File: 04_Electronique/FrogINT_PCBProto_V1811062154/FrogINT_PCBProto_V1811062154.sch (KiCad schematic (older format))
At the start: 3 parts

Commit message: Creation d'une version Draft du schéma
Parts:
- added C? (x2): 22pF, symbol Device:C
- added C? (x2): 0.1µF, symbol Device:C
- added D? (x3): WS2812B, LED_SMD:LED_WS2812B_PLCC4_5.0x5.0mm_P3.2mm, symbol LED:WS2812B
- added J?: AVR-JTAG-10, symbol Connector:AVR-JTAG-10
- added J?: USB_B_Mini, symbol Connector_FTA:USB_B_Mini
- added R?: 10k, symbol Device:R
- added SW?: SW_SPST, symbol Switch:SW_SPST
- added Y?: 16MHz, symbol Device:Crystal
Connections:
- net labels added: D+, D-, Input_Interrupt, reset
- wire segments 20 -> 82
- no-connect marks 2 -> 1
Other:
- note added: "By-Pass Cap"
- note added: "JTAG"
- note added: "LED RGB"
- moved on the sheet: R?, SW?

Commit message: Création version 01 du schéma pour impression Chine
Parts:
- added C1, C9: 22µF, symbol Device:CP
- added C10, C2, C3: 100nF, symbol Device:C
- added C8: 1µF, symbol Device:C
- added F1: Polyfuse MF-MSMF050-2, symbol Device:Polyfuse_Small
- added J2: Conn_01x01_Female, symbol Connector:Conn_01x01_Female
- added Q1, Q2: PMV48XP, symbol Device:Q_PMOS_DGS
- added R2, R3: 22, symbol Device:R
- added R4, R5: 10k, symbol Device:R
- added U1: NCP1117-5.0_SOT223, Package_TO_SOT_SMD:SOT-223-3_TabPin2, symbol Regulator_Linear:NCP1117-5.0_SOT223
- added U2: LP2985-3.3, Package_TO_SOT_SMD:SOT-23-5, symbol Regulator_Linear:LP2985-3.3
- J1: renamed from J?; symbol Connector_FTA:USB_B_Mini -> FrogINT_PCBProto_V1811062154-rescue:USB_B_Mini-Connector_FTA
- gave numbers to parts that had none: 14
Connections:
- net labels added: +5V, VBUS, Vin
- wire segments 82 -> 135
- no-connect marks 1 -> 2
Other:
- note added: "ATMEGA16U2"
- note added: "Power supply + By-Pass"
- note removed: "ATMega16U car possède USB et I2C"
- note removed: "Diamètre trou = 35mm"

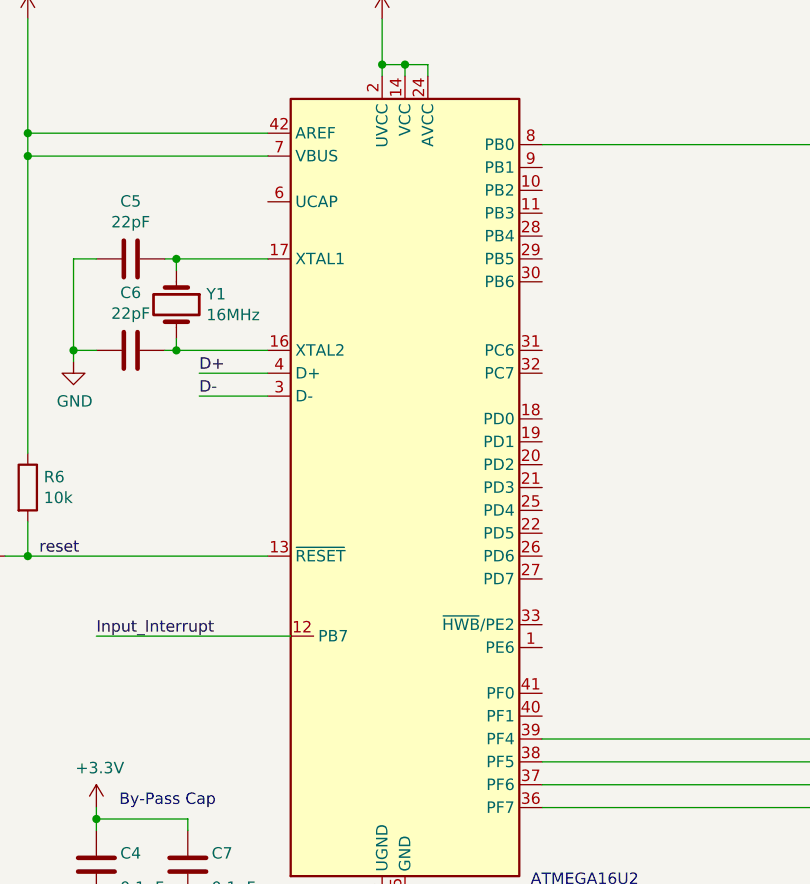
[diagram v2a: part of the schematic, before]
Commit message: First Prototype realization concerning the PCB, BOM and other manufacturing files.
This prototype could be use with Chinese partner for "Request For Quotation" process.
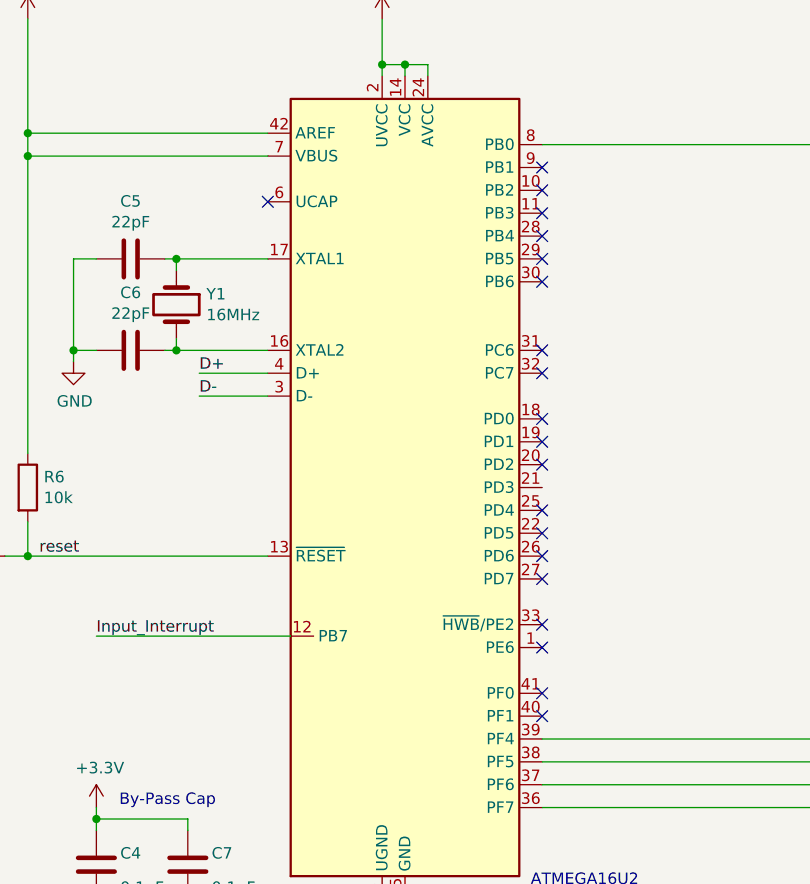
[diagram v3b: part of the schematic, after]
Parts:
- C1, C10, C2, C3, C4, C5, C6, C7, C8, C9: footprint (none) -> FTA_FrogINT_Library_Footprint_Package:CP_EIA-2012-12_Kemet-R
- D1, D2, D3: footprint LED_SMD:LED_WS2812B_PLCC4_5.0x5.0mm_P3.2mm -> FTA_FrogINT_Library_Footprint_Package:LED_WS2812B_PLCC4_5.0x5.0mm_P3.2mm
- F1: footprint (none) -> Fuse:Fuse_1206_3216Metric
- J1: footprint (none) -> Connector_USB:USB_Micro-B_Amphenol_10103594-0001LF_Horizontal
- J2: footprint (none) -> Connector_PinHeader_2.54mm:PinHeader_1x01_P2.54mm_Horizontal
- J3: footprint (none) -> FTA_FrogINT_Library_Footprint_Package:PinHeader_2x05_P2.54mm_Vertical
- Q1, Q2: footprint (none) -> Package_TO_SOT_SMD:SOT-23-6
- R1, R2, R3, R4, R5, R6: footprint (none) -> FTA_FrogINT_Library_Footprint_Package:R_0603_1608Metric
- SW1, SW2: footprint (none) -> FTA_FrogINT_Library_Footprint_Package:SW_SPST_B3S-1000
- U3: footprint Package_QFP:TQFP-44_10x10mm_P0.8mm -> FTA_FrogINT_Library_Footprint_Package:TQFP-44_10x10mm_P0.8mm
- Y1: footprint (none) -> FTA_FrogINT_Library_Footprint_Package:Crystal_HC49-U_Vertical
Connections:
- no-connect marks 2 -> 22
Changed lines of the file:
@@
 F 0 "U3" H 6100 1150 50  0000 C CNN
 F 1 "ATmega16U4RC-AU" H 6000 973 50  0001 C CNN
-F 2 "Package_QFP:TQFP-44_10x10mm_P0.8mm" H 6000 2950 50  0001 C CIN
+F 2 "FTA_FrogINT_Library_Footprint_Package:TQFP-44_10x10mm_P0.8mm" H 6000 2950 50  0001 C CIN
 F 3 "http://ww1.microchip.com/downloads/en/DeviceDoc/Atmel-7766-8-bit-AVR-ATmega16U4-32U4_Datasheet.pdf" H 6000 2950 50  0001 C CNN
 	1    6000 2950
@@
 F 0 "SW2" H 4050 3393 50  0000 C CNN
 F 1 "SW_SPST" H 4050 3394 50  0001 C CNN
-F 2 "" H 4050 3250 50  0001 C CNN
+F 2 "FTA_FrogINT_Library_Footprint_Package:SW_SPST_B3S-1000" H 4050 3250 50  0001 C CNN
 F 3 "" H 4050 3250 50  0001 C CNN
 	1    4050 3250
@@
 F 0 "R6" H 4420 2996 50  0000 L CNN
 F 1 "10k" H 4420 2905 50  0000 L CNN
-F 2 "" V 4280 2950 50  0001 C CNN
+F 2 "FTA_FrogINT_Library_Footprint_Package:R_0603_1608Metric" V 4280 2950 50  0001 C CNN
 F 3 "~" H 4350 2950 50  0001 C CNN
 	1    4350 2950
@@
 F 0 "SW1" H 1100 1893 50  0000 C CNN
 F 1 "SW_SPST" H 1100 1894 50  0001 C CNN
-F 2 "" H 1100 1750 50  0001 C CNN
+F 2 "FTA_FrogINT_Library_Footprint_Package:SW_SPST_B3S-1000" H 1100 1750 50  0001 C CNN
 F 3 "" H 1100 1750 50  0001 C CNN
 	1    1100 1750
@@
 F 0 "R1" H 1370 1396 50  0000 L CNN
 F 1 "10k" H 1370 1305 50  0000 L CNN
-F 2 "" V 1230 1350 50  0001 C CNN
+F 2 "FTA_FrogINT_Library_Footprint_Package:R_0603_1608Metric" V 1230 1350 50  0001 C CNN
 F 3 "~" H 1300 1350 50  0001 C CNN
 	1    1300 1350
@@
 F 0 "J3" H 9621 4196 50  0000 R CNN
 F 1 "AVR-JTAG-10" H 9621 4105 50  0000 R CNN
-F 2 "" V 9850 4300 50  0001 C CNN
+F 2 "FTA_FrogINT_Library_Footprint_Package:PinHeader_2x05_P2.54mm_Vertical" V 9850 4300 50  0001 C CNN
 F 3 " ~" H 8725 3600 50  0001 C CNN
 	1    10000 4150
@@
 F 0 "D1" H 8991 1496 50  0000 L CNN
 F 1 "WS2812B" H 8700 1200 50  0000 L CNN
-F 2 "LED_SMD:LED_WS2812B_PLCC4_5.0x5.0mm_P3.2mm" H 8700 1150 50  0001 L TNN
+F 2 "FTA_FrogINT_Library_Footprint_Package:LED_WS2812B_PLCC4_5.0x5.0mm_P3.2mm" H 8700 1150 50  0001 L TNN
 F 3 "https://cdn-shop.adafruit.com/datasheets/WS2812B.pdf" H 8750 1075 50  0001 L TNN
 	1    8650 1450
@@
 F 0 "D2" H 9791 1496 50  0000 L CNN
 F 1 "WS2812B" H 9500 1200 50  0000 L CNN
-F 2 "LED_SMD:LED_WS2812B_PLCC4_5.0x5.0mm_P3.2mm" H 9500 1150 50  0001 L TNN
+F 2 "FTA_FrogINT_Library_Footprint_Package:LED_WS2812B_PLCC4_5.0x5.0mm_P3.2mm" H 9500 1150 50  0001 L TNN
 F 3 "https://cdn-shop.adafruit.com/datasheets/WS2812B.pdf" H 9550 1075 50  0001 L TNN
 	1    9450 1450
@@
 F 0 "D3" H 10591 1496 50  0000 L CNN
 F 1 "WS2812B" H 10300 1200 50  0000 L CNN
-F 2 "LED_SMD:LED_WS2812B_PLCC4_5.0x5.0mm_P3.2mm" H 10300 1150 50  0001 L TNN
+F 2 "FTA_FrogINT_Library_Footprint_Package:LED_WS2812B_PLCC4_5.0x5.0mm_P3.2mm" H 10300 1150 50  0001 L TNN
 F 3 "https://cdn-shop.adafruit.com/datasheets/WS2812B.pdf" H 10350 1075 50  0001 L TNN
 	1    10250 1450
@@
 F 0 "Y1" V 4954 2281 50  0000 L CNN
 F 1 "16MHz" V 5045 2281 50  0000 L CNN
-F 2 "" H 5000 2150 50  0001 C CNN
+F 2 "FTA_FrogINT_Library_Footprint_Package:Crystal_HC49-U_Vertical" H 5000 2150 50  0001 C CNN
 F 3 "~" H 5000 2150 50  0001 C CNN
 	1    5000 2150
@@
 F 0 "C5" V 4548 1950 50  0000 C CNN
 F 1 "22pF" V 4639 1950 50  0000 C CNN
-F 2 "" H 4838 1800 50  0001 C CNN
+F 2 "FTA_FrogINT_Library_Footprint_Package:CP_EIA-2012-12_Kemet-R" H 4838 1800 50  0001 C CNN
 F 3 "~" H 4800 1950 50  0001 C CNN
 	1    4800 1950
@@
 F 0 "C6" V 4548 2350 50  0000 C CNN
 F 1 "22pF" V 4639 2350 50  0000 C CNN
-F 2 "" H 4838 2200 50  0001 C CNN
+F 2 "FTA_FrogINT_Library_Footprint_Package:CP_EIA-2012-12_Kemet-R" H 4838 2200 50  0001 C CNN
 F 3 "~" H 4800 2350 50  0001 C CNN
 	1    4800 2350
@@
 F 0 "J1" H 855 5367 50  0000 C CNN
 F 1 "USB_B_Mini" H 855 5276 50  0000 C CNN
-F 2 "" H 950 4850 50  0001 C CNN
+F 2 "Connector_USB:USB_Micro-B_Amphenol_10103594-0001LF_Horizontal" H 950 4850 50  0001 C CNN
 F 3 "~" H 950 4850 50  0001 C CNN
 	1    800  4900
@@
 F 0 "C4" H 4500 4550 50  0000 C CNN
 F 1 "0.1µF" H 4450 4700 50  0000 C CNN
-F 2 "" H 4688 4450 50  0001 C CNN
+F 2 "FTA_FrogINT_Library_Footprint_Package:CP_EIA-2012-12_Kemet-R" H 4688 4450 50  0001 C CNN
 F 3 "~" H 4650 4600 50  0001 C CNN
 	1    4650 4600
@@
 F 0 "C7" H 4900 4550 50  0000 C CNN
 F 1 "0.1µF" H 4850 4700 50  0000 C CNN
-F 2 "" H 5088 4450 50  0001 C CNN
+F 2 "FTA_FrogINT_Library_Footprint_Package:CP_EIA-2012-12_Kemet-R" H 5088 4450 50  0001 C CNN
 F 3 "~" H 5050 4600 50  0001 C CNN
 	1    5050 4600
@@
 F 0 "Q2" V 2800 6750 50  0000 C CNN
 F 1 "PMV48XP" V 2891 6750 50  0000 C CNN
-F 2 "" H 2750 6850 50  0001 C CNN
+F 2 "Package_TO_SOT_SMD:SOT-23-6" H 2750 6850 50  0001 C CNN
 F 3 "~" H 2550 6750 50  0001 C CNN
 	1    2550 6750
@@
 F 0 "R4" H 2170 7096 50  0000 L CNN
 F 1 "10k" H 2170 7005 50  0000 L CNN
-F 2 "" V 2030 7050 50  0001 C CNN
+F 2 "FTA_FrogINT_Library_Footprint_Package:R_0603_1608Metric" V 2030 7050 50  0001 C CNN
 F 3 "~" H 2100 7050 50  0001 C CNN
 	1    2100 7050
@@
 F 0 "C3" H 2950 7050 50  0000 C CNN
 F 1 "100nF" H 2900 7200 50  0000 C CNN
-F 2 "" H 3138 6950 50  0001 C CNN
+F 2 "FTA_FrogINT_Library_Footprint_Package:CP_EIA-2012-12_Kemet-R" H 3138 6950 50  0001 C CNN
 F 3 "~" H 3100 7100 50  0001 C CNN
 	1    3100 7100
@@
 F 0 "C10" H 6300 6950 50  0000 C CNN
 F 1 "100nF" H 6250 7100 50  0000 C CNN
-F 2 "" H 6488 6850 50  0001 C CNN
+F 2 "FTA_FrogINT_Library_Footprint_Package:CP_EIA-2012-12_Kemet-R" H 6488 6850 50  0001 C CNN
 F 3 "~" H 6450 7000 50  0001 C CNN
 	1    6450 7000
@@
 F 0 "C9" H 6168 7046 50  0000 L CNN
 F 1 "22µF" H 6150 6900 50  0000 L CNN
-F 2 "" H 6088 6850 50  0001 C CNN
+F 2 "FTA_FrogINT_Library_Footprint_Package:CP_EIA-2012-12_Kemet-R" H 6088 6850 50  0001 C CNN
 F 3 "~" H 6050 7000 50  0001 C CNN
 	1    6050 7000
@@
 F 0 "C8" H 5300 7050 50  0000 C CNN
 F 1 "1µF" H 5250 7200 50  0000 C CNN
-F 2 "" H 5488 6950 50  0001 C CNN
+F 2 "FTA_FrogINT_Library_Footprint_Package:CP_EIA-2012-12_Kemet-R" H 5488 6950 50  0001 C CNN
 F 3 "~" H 5450 7100 50  0001 C CNN
 	1    5450 7100
@@
 F 0 "Q1" V 1450 6750 50  0000 C CNN
 F 1 "PMV48XP" V 1541 6750 50  0000 C CNN
-F 2 "" H 1400 6850 50  0001 C CNN
+F 2 "Package_TO_SOT_SMD:SOT-23-6" H 1400 6850 50  0001 C CNN
 F 3 "~" H 1200 6750 50  0001 C CNN
 	1    1200 6750
@@
 F 0 "J2" V 1140 5962 50  0000 R CNN
 F 1 "Conn_01x01_Female" V 1049 5962 50  0000 R CNN
-F 2 "" H 1200 6050 50  0001 C CNN
+F 2 "Connector_PinHeader_2.54mm:PinHeader_1x01_P2.54mm_Horizontal" H 1200 6050 50  0001 C CNN
 F 3 "~" H 1200 6050 50  0001 C CNN
 	1    1200 6050
@@
 F 0 "R2" V 1200 4850 50  0000 L CNN
 F 1 "22" V 1400 4850 50  0000 L CNN
-F 2 "" V 1230 4900 50  0001 C CNN
+F 2 "FTA_FrogINT_Library_Footprint_Package:R_0603_1608Metric" V 1230 4900 50  0001 C CNN
 F 3 "~" H 1300 4900 50  0001 C CNN
 	1    1300 4900
@@
 F 0 "R3" V 1550 4950 50  0000 L CNN
 F 1 "22" V 1750 4950 50  0000 L CNN
-F 2 "" V 1580 5000 50  0001 C CNN
+F 2 "FTA_FrogINT_Library_Footprint_Package:R_0603_1608Metric" V 1580 5000 50  0001 C CNN
 F 3 "~" H 1650 5000 50  0001 C CNN
 	1    1650 5000
@@
 F 0 "F1" V 1395 4700 50  0000 C CNN
 F 1 "Polyfuse MF-MSMF050-2" V 1486 4700 50  0000 C CNN
-F 2 "" H 1650 4500 50  0001 L CNN
+F 2 "Fuse:Fuse_1206_3216Metric" H 1650 4500 50  0001 L CNN
 F 3 "~" H 1600 4700 50  0001 C CNN
 	1    1600 4700
@@
 F 0 "C2" H 1800 3800 50  0000 C CNN
 F 1 "100nF" H 1750 3950 50  0000 C CNN
-F 2 "" H 1988 3700 50  0001 C CNN
+F 2 "FTA_FrogINT_Library_Footprint_Package:CP_EIA-2012-12_Kemet-R" H 1988 3700 50  0001 C CNN
 F 3 "~" H 1950 3850 50  0001 C CNN
 	1    1950 3850
@@
 F 0 "C1" H 1618 3896 50  0000 L CNN
 F 1 "22µF" H 1600 3750 50  0000 L CNN
-F 2 "" H 1538 3700 50  0001 C CNN
+F 2 "FTA_FrogINT_Library_Footprint_Package:CP_EIA-2012-12_Kemet-R" H 1538 3700 50  0001 C CNN
 F 3 "~" H 1500 3850 50  0001 C CNN
 	1    1500 3850
@@
 F 0 "R5" H 2420 3896 50  0000 L CNN
 F 1 "10k" H 2420 3805 50  0000 L CNN
-F 2 "" V 2280 3850 50  0001 C CNN
+F 2 "FTA_FrogINT_Library_Footprint_Package:R_0603_1608Metric" V 2280 3850 50  0001 C CNN
 F 3 "~" H 2350 3850 50  0001 C CNN
 	1    2350 3850
@@
 Text Notes 6550 4700 0    50   ~ 0
 ATMEGA16U2
+NoConn ~ 6600 3950
+NoConn ~ 6600 3850
+NoConn ~ 6600 3650
+NoConn ~ 6600 3550
+NoConn ~ 6600 3350
+NoConn ~ 6600 3250
+NoConn ~ 6600 3150
+NoConn ~ 6600 3050
+NoConn ~ 6600 2850
+NoConn ~ 6600 2750
+NoConn ~ 6600 2650
+NoConn ~ 6600 2450
+NoConn ~ 6600 2350
+NoConn ~ 6600 2050
+NoConn ~ 6600 1950
+NoConn ~ 6600 1850
+NoConn ~ 6600 1750
+NoConn ~ 6600 1650
+NoConn ~ 6600 1550
+NoConn ~ 5400 1700
 $EndSCHEMATC

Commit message: Creation d'un touch Pad et Ajout du composant TTP223.
Création des librairies équivalentes pour le pad dans Samsac.
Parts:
- added C11: 22pF, FTA_FrogINT_Library_Footprint_Package:CP_EIA-2012-12_Kemet-R, symbol Device:C
- added C12: 100nF, FTA_FrogINT_Library_Footprint_Package:CP_EIA-2012-12_Kemet-R, symbol Device:C
- added IC1: TTP223-BA6, SamacSys_Parts:SOT95P285X126-6N, symbol SamacSys_Parts:TTP223-BA6
- added U4: TouchSensePanel, SamacSys_PCB_Library:TouchSensePad, symbol SamacSys_Parts:TouchSensePanel
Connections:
- net labels added: Cap-TouchSensor, Input_Int_Touch
- wire segments 135 -> 155
- no-connect marks 22 -> 21
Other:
- note added: "Touch Sense"
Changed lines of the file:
@@
 $EndDescr
-$Comp
-L FrogINT_PCBProto_V1811062154-cache:ATmega16U4RC-AU U3
-U 1 1 5BE236C9
-P 6000 2950
-F 0 "U3" H 6100 1150 50  0000 C CNN
-F 1 "ATmega16U4RC-AU" H 6000 973 50  0001 C CNN
-F 2 "FTA_FrogINT_Library_Footprint_Package:TQFP-44_10x10mm_P0.8mm" H 6000 2950 50  0001 C CIN
-F 3 "http://ww1.microchip.com/downloads/en/DeviceDoc/Atmel-7766-8-bit-AVR-ATmega16U4-32U4_Datasheet.pdf" H 6000 2950 50  0001 C CNN
-	1    6000 2950
-	1    0    0    -1
-$EndComp
 $Comp
 L power:+3.3V #PWR021
@@
 	9350 3950 9100 3950
 $Comp
-L power:GND #PWR028
+L power:GND #PWR029
 U 1 1 5BEAA0D2
 P 10000 4850
-F 0 "#PWR028" H 10000 4600 50  0001 C CNN
+F 0 "#PWR029" H 10000 4600 50  0001 C CNN
 F 1 "GND" H 10005 4677 50  0000 C CNN
 F 2 "" H 10000 4850 50  0001 C CNN
@@
 	10950 5100 9050 5100
 $Comp
-L power:+3.3V #PWR027
+L power:+3.3V #PWR028
 U 1 1 5BEAB64E
 P 10000 3450
-F 0 "#PWR027" H 10000 3300 50  0001 C CNN
+F 0 "#PWR028" H 10000 3300 50  0001 C CNN
 F 1 "+3.3V" H 10015 3623 50  0000 C CNN
 F 2 "" H 10000 3450 50  0001 C CNN
@@
 NoConn ~ 6600 2450
 NoConn ~ 6600 2350
-NoConn ~ 6600 2050
 NoConn ~ 6600 1950
 NoConn ~ 6600 1850
@@
 NoConn ~ 6600 1550
 NoConn ~ 5400 1700
+$Comp
+L FrogINT_PCBProto_V1811062154-cache:ATmega16U4RC-AU U3
+U 1 1 5BE236C9
+P 6000 2950
+F 0 "U3" H 6100 1150 50  0000 C CNN
+F 1 "ATmega16U4RC-AU" H 6000 973 50  0001 C CNN
+F 2 "FTA_FrogINT_Library_Footprint_Package:TQFP-44_10x10mm_P0.8mm" H 6000 2950 50  0001 C CIN
+F 3 "http://ww1.microchip.com/downloads/en/DeviceDoc/Atmel-7766-8-bit-AVR-ATmega16U4-32U4_Datasheet.pdf" H 6000 2950 50  0001 C CNN
+	1    6000 2950
+	1    0    0    -1
+$EndComp
+Wire Wire Line
+	6600 2050 7200 2050
+Text Label 6800 2050 0    50   ~ 0
+Input_Int_Touch
+Text Label 8250 5700 0    50   ~ 0
+Input_Int_Touch
+Wire Wire Line
+	8850 5700 8250 5700
+Wire Wire Line
+	8850 5800 8450 5800
+Text Label 7700 5800 0    50   ~ 0
+Cap-TouchSensor
+$Comp
+L power:GND #PWR027
+U 1 1 5C375D63
+P 8750 6250
+F 0 "#PWR027" H 8750 6000 50  0001 C CNN
+F 1 "GND" H 8755 6077 50  0000 C CNN
+F 2 "" H 8750 6250 50  0001 C CNN
+F 3 "" H 8750 6250 50  0001 C CNN
+	1    8750 6250
+	1    0    0    -1
+$EndComp
+Wire Wire Line
+	8850 5900 8750 5900
+Wire Wire Line
+	8750 5900 8750 6200
+$Comp
+L Device:C C11
+U 1 1 5C37BB9A
+P 8450 6000
+F 0 "C11" H 8300 5950 50  0000 C CNN
+F 1 "22pF" H 8250 6100 50  0000 C CNN
+F 2 "FTA_FrogINT_Library_Footprint_Package:CP_EIA-2012-12_Kemet-R" H 8488 5850 50  0001 C CNN
+F 3 "~" H 8450 6000 50  0001 C CNN
+	1    8450 6000
+	-1   0    0    1
+$EndComp
+Wire Wire Line
+	8450 5850 8450 5800
+Connection ~ 8450 5800
+Wire Wire Line
+	8450 5800 7550 5800
+Wire Wire Line
+	8450 6150 8450 6200
+Wire Wire Line
+	8450 6200 8750 6200
+Connection ~ 8750 6200
+Wire Wire Line
+	8750 6200 8750 6250
+$Comp
+L SamacSys_Parts:TTP223-BA6 IC1
+U 1 1 5C3A6478
+P 8850 5700
+F 0 "IC1" H 9400 5965 50  0000 C CNN
+F 1 "TTP223-BA6" H 9400 5874 50  0000 C CNN
+F 2 "SamacSys_Parts:SOT95P285X126-6N" H 9800 5800 50  0001 L CNN
+F 3 "https://radiokot.ru/konkursCatDay2014/53/01.pdf" H 9800 5700 50  0001 L CNN
+F 4 "1 KEY TOUCH PAD DETECTOR IC" H 9800 5600 50  0001 L CNN "Description"
+F 5 "1.26" H 9800 5500 50  0001 L CNN "Height"
+F 6 "TONTEK" H 9800 5400 50  0001 L CNN "Manufacturer_Name"
+F 7 "TTP223-BA6" H 9800 5300 50  0001 L CNN "Manufacturer_Part_Number"
+F 8 "" H 9800 5200 50  0001 L CNN "RS Part Number"
+F 9 "" H 9800 5100 50  0001 L CNN "RS Price/Stock"
+F 10 "" H 9800 5000 50  0001 L CNN "Mouser Part Number"
+F 11 "" H 9800 4900 50  0001 L CNN "Mouser Price/Stock"
+	1    8850 5700
+	1    0    0    -1
+$EndComp
+$Comp
+L power:GND #PWR030
+U 1 1 5C3A6566
+P 10050 6250
+F 0 "#PWR030" H 10050 6000 50  0001 C CNN
+F 1 "GND" H 10055 6077 50  0000 C CNN
+F 2 "" H 10050 6250 50  0001 C CNN
+F 3 "" H 10050 6250 50  0001 C CNN
+	1    10050 6250
+	1    0    0    -1
+$EndComp
+Wire Wire Line
+	9950 5900 10050 5900
+Wire Wire Line
+	10050 5900 10050 6200
+Wire Wire Line
+	9950 5800 10050 5800
+Wire Wire Line
+	10050 5800 10050 5900
+Connection ~ 10050 5900
+$Comp
+L power:+5V #PWR031
+U 1 1 5C3B3123
+P 10300 5600
+F 0 "#PWR031" H 10300 5450 50  0001 C CNN
+F 1 "+5V" H 10315 5773 50  0000 C CNN
+F 2 "" H 10300 5600 50  0001 C CNN
+F 3 "" H 10300 5600 50  0001 C CNN
+	1    10300 5600
+	1    0    0    -1
+$EndComp
+Wire Wire Line
+	9950 5700 10300 5700
+$Comp
+L Device:C C12
+U 1 1 5C3B9993
+P 10300 5950
+F 0 "C12" H 10150 5900 50  0000 C CNN
+F 1 "100nF" H 10100 6050 50  0000 C CNN
+F 2 "FTA_FrogINT_Library_Footprint_Package:CP_EIA-2012-12_Kemet-R" H 10338 5800 50  0001 C CNN
+F 3 "~" H 10300 5950 50  0001 C CNN
+	1    10300 5950
+	-1   0    0    1
+$EndComp
+Wire Wire Line
+	10300 5700 10300 5600
+Wire Wire Line
+	10300 5800 10300 5700
+Connection ~ 10300 5700
+Wire Wire Line
+	10300 6100 10300 6200
+Wire Wire Line
+	10300 6200 10050 6200
+Connection ~ 10050 6200
+Wire Wire Line
+	10050 6200 10050 6250
+Wire Notes Line
+	6950 5200 10950 5200
+Wire Notes Line
+	10950 5200 10950 6500
+Wire Notes Line
+	10950 6500 6950 6500
+Wire Notes Line
+	6950 6500 6950 5200
+Text Notes 6950 5300 0    50   ~ 0
+Touch Sense
+$Comp
+L SamacSys_Parts:TouchSensePanel U4
+U 1 1 5C40483E
+P 7350 5800
+F 0 "U4" H 7339 5535 50  0000 C CNN
+F 1 "TouchSensePanel" H 7339 5626 50  0000 C CNN
+F 2 "SamacSys_PCB_Library:TouchSensePad" H 7350 5800 50  0001 C CNN
+F 3 "" H 7350 5800 50  0001 C CNN
+	1    7350 5800
+	-1   0    0    1
+$EndComp
 $EndSCHEMATC

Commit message: ***Commit du 14/01/2019 suite aux modifications du 11/01/2019
            • Création d'un nouveau composant (schéma + PCB) TouchSense sur la librairie FTA (et non plus Samacsys)
	• Ajout de ce composant dans le design courant
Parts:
- removed U4: TouchSensePanel, SamacSys_PCB_Library:TouchSensePad, symbol SamacSys_Parts:TouchSensePanel
- added TS1: TouchSense, FTA_FrogINT_Library_Footprint_Package:CapacitiveTouchSense_Bottom_10mm, symbol FTA_FrogINT_library:TouchSense
- IC1: symbol SamacSys_Parts:TTP223-BA6 -> FrogINT_PCBProto_V1811062154-rescue:TTP223-BA6-SamacSys_Parts
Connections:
- no-connect marks 21 -> 22
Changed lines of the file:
@@
 Wire Wire Line
 	8850 5800 8450 5800
-Text Label 7700 5800 0    50   ~ 0
+Text Label 7850 5800 0    50   ~ 0
 Cap-TouchSensor
 $Comp
@@
 Connection ~ 8450 5800
 Wire Wire Line
-	8450 5800 7550 5800
+	8450 5800 7800 5800
 Wire Wire Line
 	8450 6150 8450 6200
@@
 	8750 6200 8750 6250
 $Comp
-L SamacSys_Parts:TTP223-BA6 IC1
+L FrogINT_PCBProto_V1811062154-rescue:TTP223-BA6-SamacSys_Parts IC1
 U 1 1 5C3A6478
 P 8850 5700
@@
 Touch Sense
 $Comp
-L SamacSys_Parts:TouchSensePanel U4
-U 1 1 5C40483E
-P 7350 5800
-F 0 "U4" H 7339 5535 50  0000 C CNN
-F 1 "TouchSensePanel" H 7339 5626 50  0000 C CNN
-F 2 "SamacSys_PCB_Library:TouchSensePad" H 7350 5800 50  0001 C CNN
-F 3 "" H 7350 5800 50  0001 C CNN
-	1    7350 5800
-	-1   0    0    1
+L FTA_FrogINT_library:TouchSense TS1
+U 1 1 5C39FC70
+P 7400 5800
+F 0 "TS1" H 7456 6265 50  0000 C CNN
+F 1 "TouchSense" H 7456 6174 50  0000 C CNN
+F 2 "FTA_FrogINT_Library_Footprint_Package:CapacitiveTouchSense_Bottom_10mm" H 7400 5800 50  0001 C CNN
+F 3 "" H 7400 5800 50  0001 C CNN
+	1    7400 5800
+	1    0    0    -1
 $EndComp
+NoConn ~ 6600 2950
 $EndSCHEMATC
